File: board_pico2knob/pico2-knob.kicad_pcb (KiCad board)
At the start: 2 copper layers, 53.7 x 99.5 mm, 34 parts, among them J2 LiPo_JST_PH, J3 ER-CON20HT-1, Q1 DMG3415U, SW1 SW_Push, SW2 SW_Push, SW3 SW_Push, U1 nice!nano_v2, U2 MC34063AD

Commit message: finished pcb? erc/drc passing, need export
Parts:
- removed TP5: TestPoint, TestPoint:TestPoint_Pad_D1.5mm
- C2, C4, D1, L1, R2: moved to B.Cu
- TP4: value TestPoint -> +12V
- moved R7 255.0 mm to (119.0, 171.6), turned to 90 degrees
- moved R5 253.6 mm to (115.0, 172.8)
- moved L1 251.7 mm to (99.0, 155.9), turned to -90 degrees
- moved U2 246.0 mm to (106.5, 165.9)
- moved C1 238.4 mm to (103.0, 171.0), turned to 180 degrees
- moved D1 233.7 mm to (99.0, 145.0), turned to -90 degrees
- moved R3 227.3 mm to (102.5, 129.9), turned to -90 degrees
- moved C2 217.8 mm to (95.5, 140.0), turned to -90 degrees
- moved C6 216.1 mm to (111.0, 171.0)
- moved R4 209.4 mm to (109.2, 139.0), turned to -150 degrees
- moved Q1 179.7 mm to (125.8, 168.7), turned to 45 degrees
- moved C3 178.6 mm to (130.2, 172.0), turned to 0 degrees
- moved R8 168.0 mm to (128.4, 158.6), turned to -135 degrees
- moved H3 142.0 mm to (179.0, 108.0)
- moved H4 142.0 mm to (180.0, 129.5)
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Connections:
- C3 pad 1: Net-(C3-Pad1) -> Net-(U2-Vin)
- C3 pad 2: unconnected-(C3-Pad2) -> GND
- C6 pad 1: unconnected-(C6-Pad1) -> Net-(U2-Vin)
- D1 pad 1: unconnected-(D1-K-Pad1) -> +12V
- J3 pad 1: Net-(J3-Pin_1) -> +12V
- J3 pad 10: Net-(J3-Pin_10) -> +3.3V
- J3 pad 11: unconnected-(J3-Pin_11-Pad11) -> +3.3V
- J3 pad 20: Net-(J3-Pin_20) -> GND
- J3 pad 5: Net-(J3-Pin_5) -> GND
- L1 pad 2: Net-(L1-Pad2) -> Net-(U2-Ipk)
- Q1 pad S: Net-(C3-Pad1) -> Net-(U2-Vin)
- R1 pad 2: unconnected-(R1-Pad2) -> GND
- R2 pad 2: unconnected-(R2-Pad2) -> /OLED_RES
- R3 pad 1: unconnected-(R3-Pad1) -> +12V
- R3 pad 2: Net-(R3-Pad2) -> Net-(U2-Vfb)
- R4 pad 1: Net-(R3-Pad2) -> Net-(U2-Vfb)
- R5 pad 2: Net-(L1-Pad2) -> Net-(U2-Ipk)
- R6 pad 2: unconnected-(R6-Pad2) -> /OLED_CS
- R7 pad 1: unconnected-(R7-Pad1) -> Net-(U2-Ipk)
- RE1 pad S1: unconnected-(RE1-PadS1) -> /ENC_SW
- RE1 pad S2: unconnected-(RE1-PadS2) -> GND
- TP1 pad 1: unconnected-(TP1-Pad1) -> GND
- TP2 pad 1: unconnected-(TP2-Pad1) -> +BATT
- TP4 pad 1: /SCL -> +12V
- U1 pad 1: /OLED_SDI -> /OLED_DC
- U1 pad 10: /ENC_SW -> unconnected-(U1-P0.11-Pad10)
- U1 pad 11: /ENC_A -> unconnected-(U1-P1.04-LF-Pad11)
- U1 pad 12: /ENC_B -> /12V_EN
- U1 pad 17: /OLED_CS -> /BTN1
- U1 pad 18: /OLED_RES -> unconnected-(U1-P0.29-LF-Pad18)
- U1 pad 19: unconnected-(U1-P0.02-LF-Pad19) -> /BTN2
- U1 pad 20: /12V_EN -> /BTN3
- U1 pad 22: /OLED_DC -> /ENC_SW
- U1 pad 23: /OLED_SDI -> /ENC_B
- U1 pad 24: /OLED_SCLK -> /ENC_A
- U1 pad 3: unconnected-(U1-GND-Pad3) -> GND
- U1 pad 5: unconnected-(U1-P0.17-Pad5) -> /OLED_SDI
- U1 pad 7: /BTN1 -> /OLED_RES
- U1 pad 8: /BTN2 -> /OLED_CS
- U1 pad 9: /BTN3 -> unconnected-(U1-P1.00-Pad9)
- U2 pad 4: unconnected-(U2-GND-Pad4) -> GND
- U2 pad 5: unconnected-(U2-Vfb-Pad5) -> Net-(U2-Vfb)
- U2 pad 7: unconnected-(U2-Ipk-Pad7) -> Net-(U2-Ipk)
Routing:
- net +BATT: track 0.00 -> 101.1 mm, vias 0 -> 1
- net +12V: track 0.00 -> 66.0 mm
- net GND: track 0.00 -> 64.2 mm, vias 0 -> 7
- net /OLED_CS: track 0.00 -> 59.2 mm, vias 0 -> 1
- net /OLED_RES: track 0.00 -> 49.7 mm, vias 0 -> 1
- net /12V_EN: track 0.00 -> 42.2 mm
- net Net-(U2-Vfb): track 0.00 -> 40.3 mm, vias 0 -> 1
- net /ENC_SW: track 0.00 -> 37.7 mm
- net Net-(J3-Pin_6): track 0.00 -> 34.4 mm, vias 0 -> 1
- net Net-(U2-Ipk): track 0.00 -> 31.9 mm
- net /OLED_SDI: track 0.00 -> 30.5 mm, vias 0 -> 2
- net Net-(J3-Pin_2): track 0.00 -> 29.5 mm, vias 0 -> 1
- net +3.3V: track 0.00 -> 28.7 mm, vias 0 -> 2
- net Net-(U2-Vin): track 0.00 -> 28.2 mm
- net /ENC_B: track 0.00 -> 27.2 mm
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- added copper zone on B.Cu, net +12V
- added copper zone on B.Cu, net +3.3V
- added copper zone on F.Cu, net GND
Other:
- board size 53.7 x 99.5 mm -> 51 x 99.5 mm

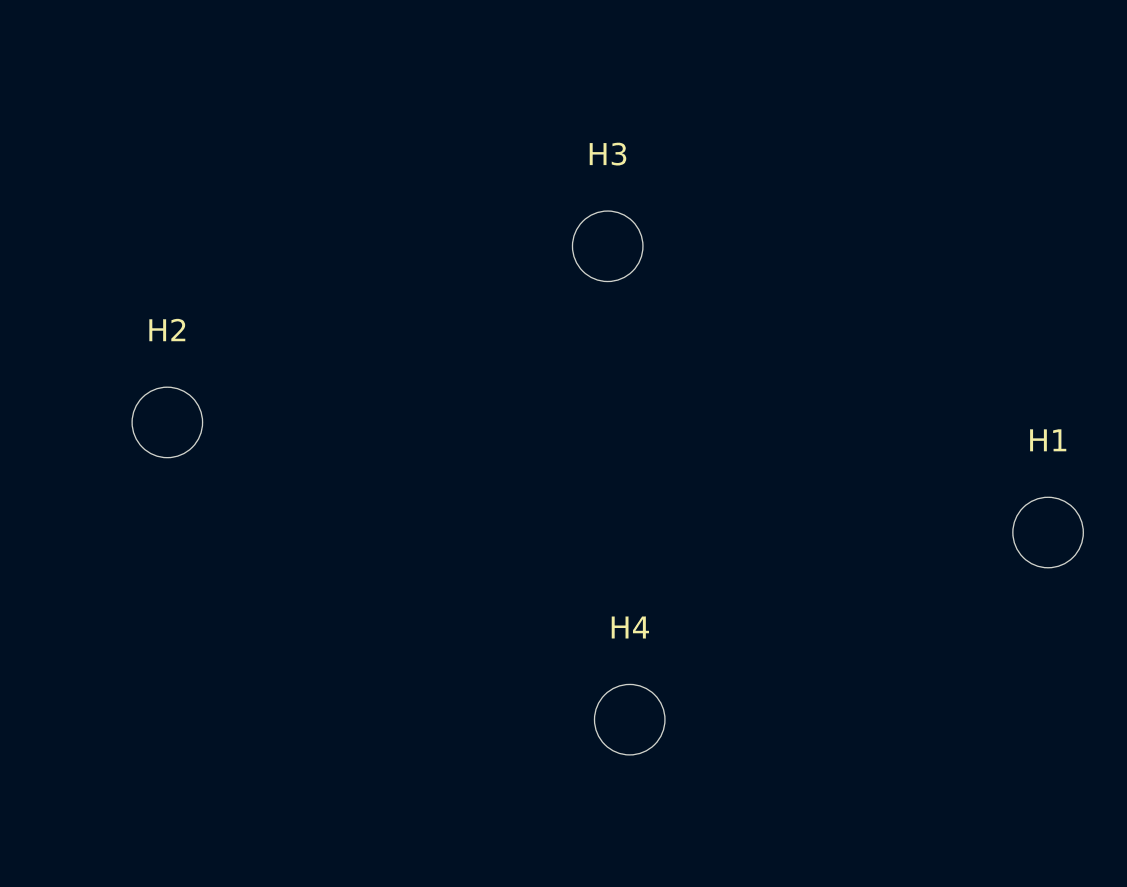
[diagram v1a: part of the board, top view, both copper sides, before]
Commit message: remove mounting holes
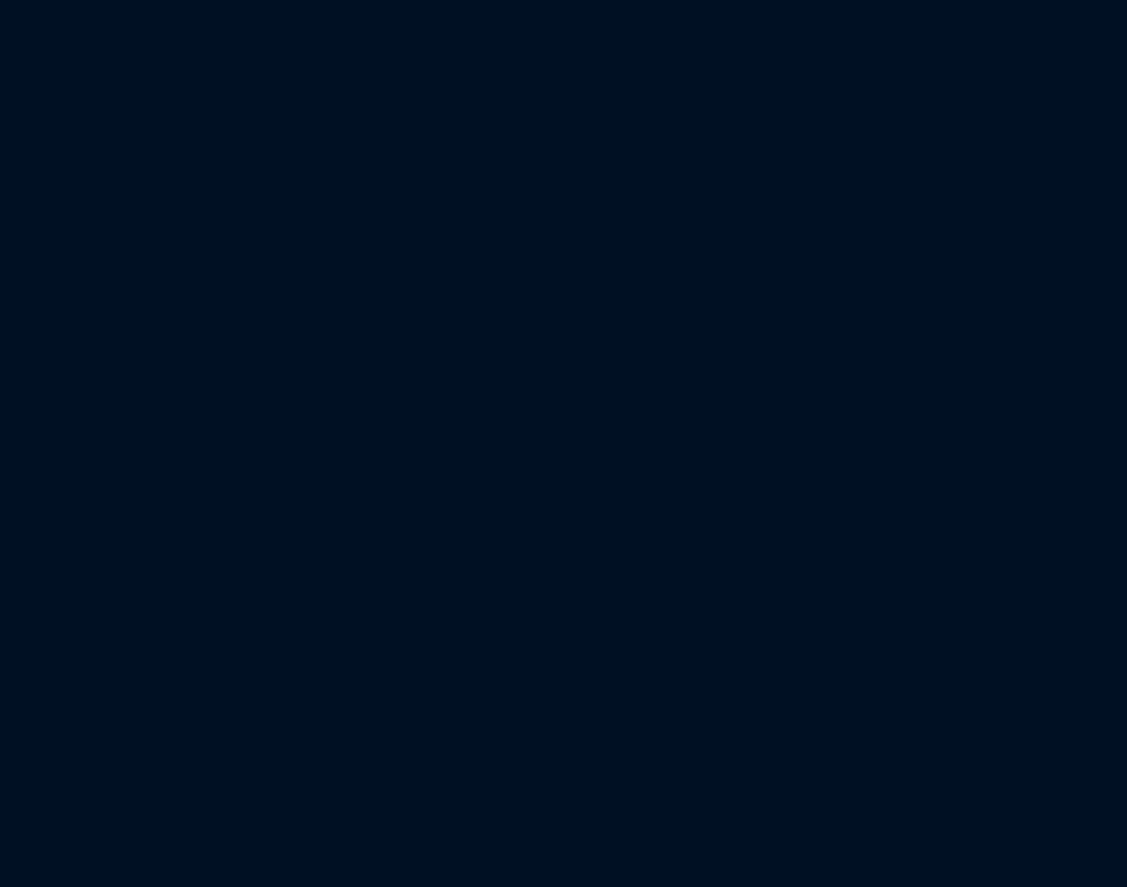
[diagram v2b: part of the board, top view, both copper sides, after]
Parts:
- removed H1, H2, H3, H4: MountingHole_3.2mm_M3, MountingHole_3.2mm_M3

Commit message: pre-U2 flip
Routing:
- net /ENC_A: track 18.3 -> 20.1 mm
- net /ENC_B: track 27.2 -> 28.4 mm
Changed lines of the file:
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@@
 	)
 	(segment
-		(start 107.5 131.085)
+		(start 111 131.875)
 		(end 108.855 129.73)
 		(width 0.2)
@@
 	(segment
 		(start 107.5 147.5)
-		(end 107.5 131.085)
+		(end 111 144)
 		(width 0.2)
 		(layer "F.Cu")
@@
 	)
 	(segment
+		(start 111 144)
+		(end 111 131.875)
+		(width 0.2)
+		(layer "F.Cu")
+		(net "/ENC_A")
+	)
+	(segment
+		(start 111.75 148.5)
+		(end 111.75 130.085)
+		(width 0.2)
+		(layer "F.Cu")
+		(net "/ENC_B")
+	)
+	(segment
+		(start 111.75 130.085)
+		(end 108.855 127.19)
+		(width 0.2)
+		(layer "F.Cu")
+		(net "/ENC_B")
+	)
+	(segment
+		(start 107.75 152.5)
+		(end 111.75 148.5)
+		(width 0.2)
+		(layer "F.Cu")
+		(net "/ENC_B")
+	)
+	(segment
 		(start 107.5 152.5)
-		(end 110.5 149.5)
-		(width 0.2)
-		(layer "F.Cu")
-		(net "/ENC_B")
-	)
-	(segment
-		(start 110.5 128.835)
-		(end 108.855 127.19)
-		(width 0.2)
-		(layer "F.Cu")
-		(net "/ENC_B")
-	)
-	(segment
-		(start 110.5 149.5)
-		(end 110.5 128.835)
+		(end 107.75 152.5)
 		(width 0.2)
 		(layer "F.Cu")
@@
 		(polygon
 			(pts
-				(xy 86 72) (xy 98.5 68.5) (xy 105.5 79) (xy 141 80.5) (xy 141 180) (xy 88 179)
+				(xy 86 72) (xy 98.5 68.5) (xy 105.5 79) (xy 141 80.5) (xy 140.5 119.75) (xy 86.88296 119.238357)
 			)
 		)
@@
 			(pts
 				(xy 103.989231 95.5) (xy 110.5 95) (xy 111.467005 82.659899) (xy 101.417367 75.254902) (xy 110 71.5)
-				(xy 116 79.5) (xy 140 103) (xy 138 122) (xy 103.5 119.5)
+				(xy 116 79.5) (xy 140 103) (xy 138.25 119.75) (xy 103.5 119.5)
 			)
 		)

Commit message: not sure bump
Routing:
- net +BATT: track 101.1 -> 103.4 mm
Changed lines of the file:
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@@
 		(start 99 143)
 		(end 99 137)
-		(width 2.5)
+		(width 1.524)
 		(layer "B.Cu")
 		(net "+12V")
@@
 		(start 99 137)
 		(end 97 135)
-		(width 2.5)
+		(width 1.524)
 		(layer "B.Cu")
 		(net "+12V")
@@
 		(start 112.475 169.090001)
 		(end 109.924999 166.54)
-		(width 0.2)
+		(width 0.6)
 		(layer "F.Cu")
 		(net "Net-(U2-Vin)")
@@
 		(start 112.475 171)
 		(end 112.475 169.090001)
-		(width 0.2)
+		(width 0.6)
 		(layer "F.Cu")
 		(net "Net-(U2-Vin)")
@@
 		(start 114.285 172.81)
 		(end 115 172.81)
-		(width 0.2)
+		(width 0.6)
 		(layer "F.Cu")
 		(net "Net-(U2-Vin)")
@@
 		(start 112.475 171)
 		(end 114.285 172.81)
-		(width 0.2)
+		(width 0.6)
 		(layer "F.Cu")
 		(net "Net-(U2-Vin)")
@@
 	)
 	(segment
+		(start 135.503472 126.051979)
+		(end 135.559318 125.987992)
+		(width 0.6)
+		(layer "B.Cu")
+		(net "+BATT")
+	)
+	(segment
+		(start 133.5 142.5)
+		(end 136.25 139.75)
+		(width 0.6)
+		(layer "B.Cu")
+		(net "+BATT")
+	)
+	(segment
+		(start 135.520826 126.30744)
+		(end 135.503472 126.051979)
+		(width 0.6)
+		(layer "B.Cu")
+		(net "+BATT")
+	)
+	(segment
 		(start 108.855 99.25)
 		(end 110.605 97.5)
@@
 	)
 	(segment
-		(start 133.5 142.5)
-		(end 133.5 137)
+		(start 135.490194 126.561653)
+		(end 135.520826 126.30744)
 		(width 0.6)
 		(layer "B.Cu")
@@
 	)
 	(segment
+		(start 135.928034 122.928034)
+		(end 131 118)
+		(width 0.6)
+		(layer "B.Cu")
+		(net "+BATT")
+	)
+	(segment
 		(start 134.5 115.5)
 		(end 134.5 113.5)
@@
 	)
 	(segment
-		(start 133.25 136.75)
-		(end 133.25 120.25)
-		(width 0.6)
-		(layer "B.Cu")
-		(net "+BATT")
-	)
-	(segment
-		(start 133.5 137)
-		(end 133.25 136.75)
+		(start 136.25 137.041336)
+		(end 135.542634 126.628462)
 		(width 0.6)
 		(layer "B.Cu")
@@
 	)
 	(segment
+		(start 136.25 139.75)
+		(end 136.25 137.041336)
+		(width 0.6)
+		(layer "B.Cu")
+		(net "+BATT")
+	)
+	(segment
 		(start 110.605 97.5)
 		(end 125.5 97.5)
@@
 	)
 	(segment
-		(start 133.25 120.25)
-		(end 131 118)
+		(start 135.559318 125.987992)
+		(end 135.928034 122.928034)
 		(width 0.6)
 		(layer "B.Cu")
@@
 		(start 126 113)
 		(end 131 118)
+		(width 0.6)
+		(layer "B.Cu")
+		(net "+BATT")
+	)
+	(segment
+		(start 135.542634 126.628462)
+		(end 135.490194 126.561653)
 		(width 0.6)
 		(layer "B.Cu")
@@
 		(polygon
 			(pts
-				(xy 74.001387 76.187716) (xy 90.5 139.5) (xy 97 139.5) (xy 100 130) (xy 100 115) (xy 100 103) (xy 100 98.5)
-				(xy 101.5 96) (xy 104 95) (xy 105.5 94.5) (xy 108.303448 91.297552) (xy 110.5 82) (xy 97 72.5)
+				(xy 74.001387 76.187716) (xy 90.5 139.5) (xy 97 139.5) (xy 99.5 131.583333) (xy 99.5 113.424397)
+				(xy 100 103) (xy 100 98.5) (xy 101.5 96) (xy 104 95) (xy 105.5 94.5) (xy 108.303448 91.297552) (xy 110.5 82)
+				(xy 97 72.5)
 			)
 		)

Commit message: passing erc/drc
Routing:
- net GND: track 64.2 -> 196.9 mm, vias 7 -> 6

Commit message: add silkscreens, copper lightning bolts export gerbers
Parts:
- added REF**: Gauge_10mm_Type2_SilkScreenTop, Calibration_Scale:Gauge_10mm_Type2_SilkScreenTop, F.Cu at (96.2, 108.3)
- added REF**: Symbol_HighVoltage_NoTriangle_2x5mm_Copper, Symbol:Symbol_HighVoltage_NoTriangle_2x5mm_Copper, F.Cu at (134.8, 128.2)
- added REF**: Symbol_HighVoltage_NoTriangle_2x5mm_Copper, Symbol:Symbol_HighVoltage_NoTriangle_2x5mm_Copper, F.Cu at (132.0, 126.2)
- added REF**: Symbol_HighVoltage_NoTriangle_2x5mm_Copper, Symbol:Symbol_HighVoltage_NoTriangle_2x5mm_Copper, F.Cu at (132.5, 131.8)
- added REF**: OSHW-Logo2_14.6x12mm_SilkScreen, Symbol:OSHW-Logo2_14.6x12mm_SilkScreen, B.Cu at (115.0, 152.8)
- R2: moved to F.Cu

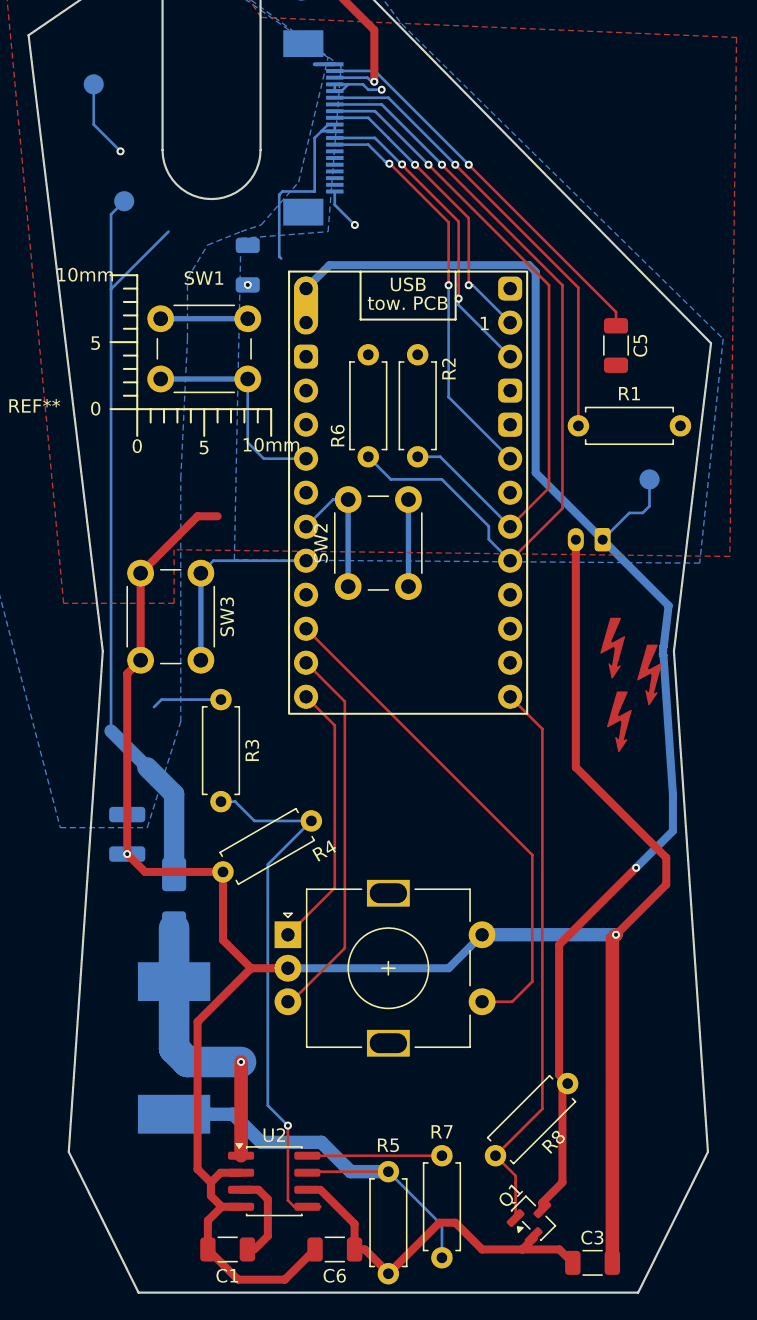
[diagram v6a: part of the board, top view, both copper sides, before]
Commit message: mounting holes, gerber export
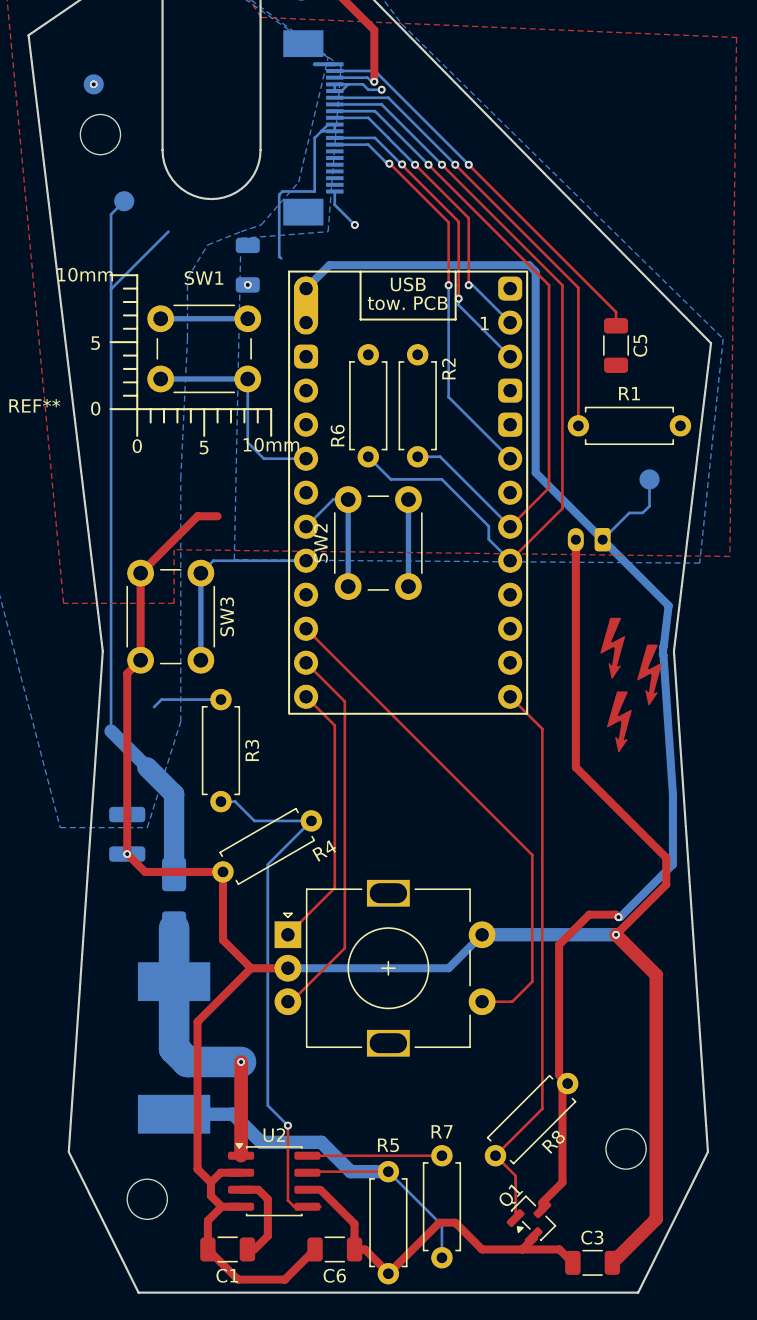
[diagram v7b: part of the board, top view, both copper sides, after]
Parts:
- added REF**: MountingHole_3mm, MountingHole:MountingHole_3mm, F.Cu at (132.8, 163.5)
- added REF**: MountingHole_3mm, MountingHole:MountingHole_3mm, F.Cu at (97.0, 167.2)
- added REF**: MountingHole_3mm, MountingHole:MountingHole_3mm, F.Cu at (93.5, 87.8)
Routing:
- net GND: track 196.9 -> 193.6 mm
- net +BATT: track 103.4 -> 105.0 mm
